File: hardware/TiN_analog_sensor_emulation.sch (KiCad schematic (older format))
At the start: 0 parts

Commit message: przeniosiono do folderu hardware
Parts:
- added H? (x4): MountingHole, symbol Mechanical:MountingHole
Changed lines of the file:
@@
 F11 "ADC7" O L 4300 4250 50
 F12 "ADC6" O L 4300 4150 50
+F13 "POTRST" O L 4300 3300 50
+F14 "POTSHDN" O L 4300 3400 50
 $EndSheet
 $Sheet
@@
 Wire Wire Line
 	3950 3150 4300 3150
+Wire Wire Line
+	3950 3300 4300 3300
+Wire Wire Line
+	4300 3400 3950 3400
+$Comp
+L Mechanical:MountingHole H?
+U 1 1 5D813031
+P 5550 1350
+F 0 "H?" H 5650 1396 50  0000 L CNN
+F 1 "MountingHole" H 5650 1305 50  0000 L CNN
+F 2 "" H 5550 1350 50  0001 C CNN
+F 3 "~" H 5550 1350 50  0001 C CNN
+	1    5550 1350
+	1    0    0    -1
+$EndComp
+$Comp
+L Mechanical:MountingHole H?
+U 1 1 5D8131EE
+P 5550 1150
+F 0 "H?" H 5650 1196 50  0000 L CNN
+F 1 "MountingHole" H 5650 1105 50  0000 L CNN
+F 2 "" H 5550 1150 50  0001 C CNN
+F 3 "~" H 5550 1150 50  0001 C CNN
+	1    5550 1150
+	1    0    0    -1
+$EndComp
+$Comp
+L Mechanical:MountingHole H?
+U 1 1 5D8138A8
+P 5550 950
+F 0 "H?" H 5650 996 50  0000 L CNN
+F 1 "MountingHole" H 5650 905 50  0000 L CNN
+F 2 "" H 5550 950 50  0001 C CNN
+F 3 "~" H 5550 950 50  0001 C CNN
+	1    5550 950
+	1    0    0    -1
+$EndComp
+$Comp
+L Mechanical:MountingHole H?
+U 1 1 5D8139A7
+P 5550 750
+F 0 "H?" H 5650 796 50  0000 L CNN
+F 1 "MountingHole" H 5650 705 50  0000 L CNN
+F 2 "" H 5550 750 50  0001 C CNN
+F 3 "~" H 5550 750 50  0001 C CNN
+	1    5550 750
+	1    0    0    -1
+$EndComp
 $EndSCHEMATC

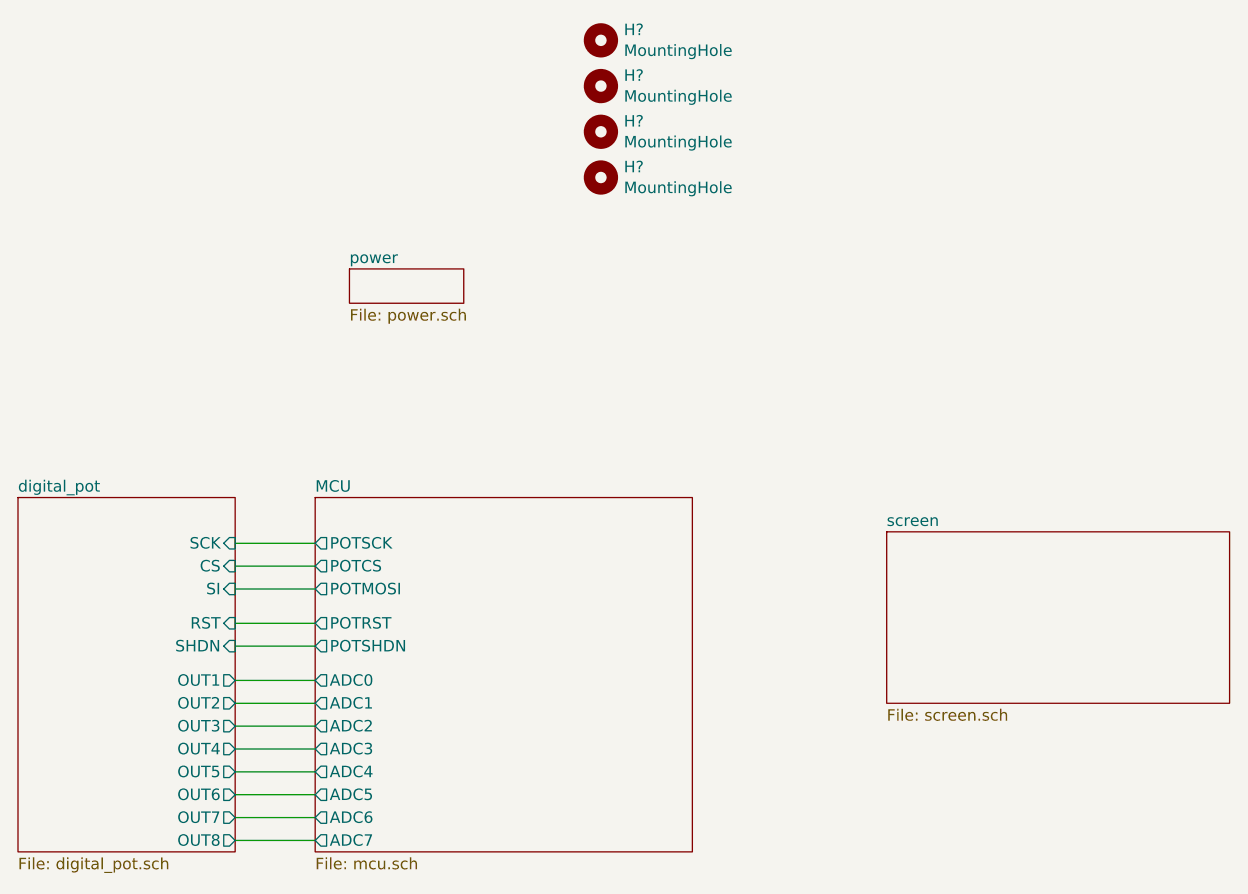
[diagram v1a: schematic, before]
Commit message: dodano wyjscie programatora, przyciski ustalono wysjcie i2c, dodany plik CubeMX z pinouterm
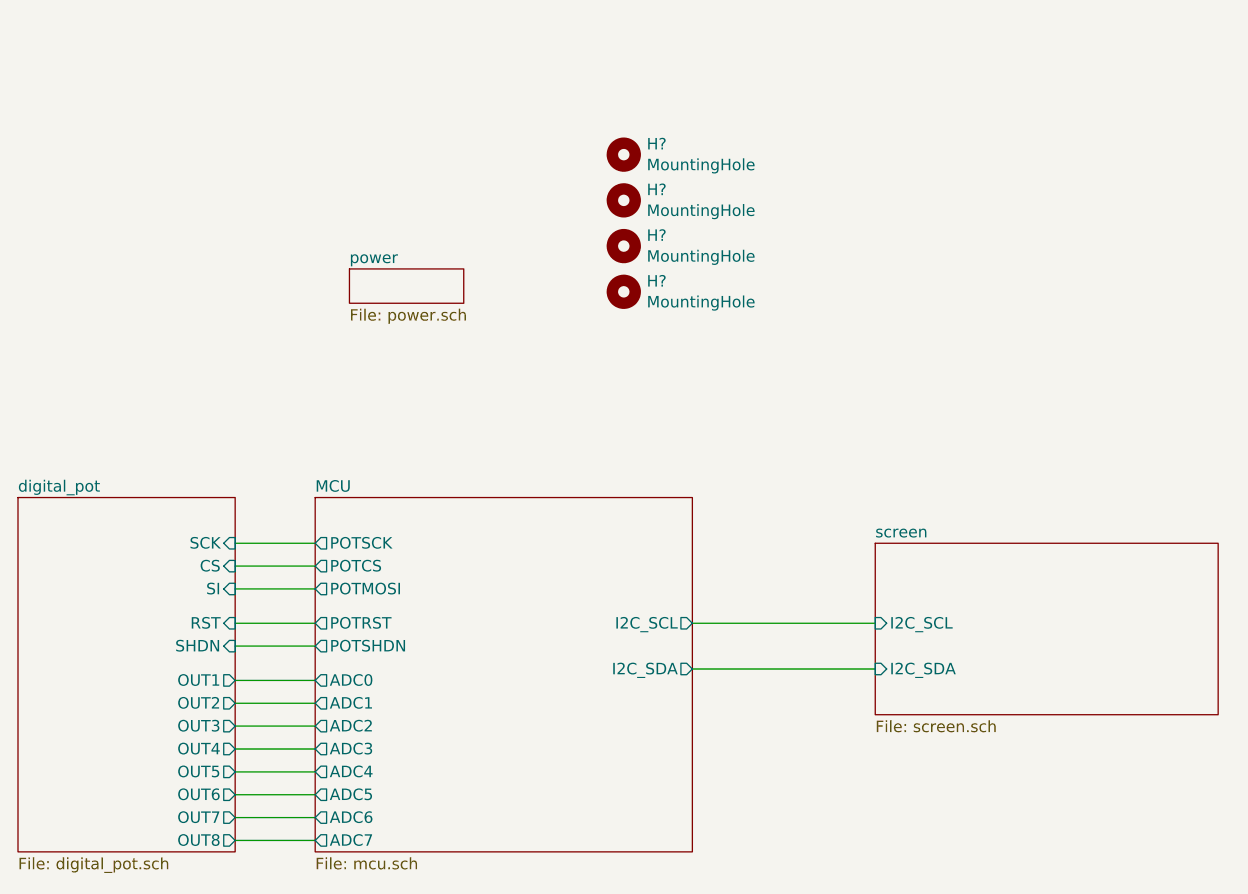
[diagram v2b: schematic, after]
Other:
- moved on the sheet: H?
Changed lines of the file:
@@
 F13 "POTRST" O L 4300 3300 50
 F14 "POTSHDN" O L 4300 3400 50
+F15 "I2C_SCL" O R 5950 3300 50
+F16 "I2C_SDA" O R 5950 3500 50
 $EndSheet
 $Sheet
@@
 $EndSheet
 $Sheet
-S 6800 2900 1500 750
+S 6750 2950 1500 750
 U 5CDEAC68
 F0 "screen" 50
 F1 "screen.sch" 50
+F2 "I2C_SCL" I L 6750 3300 50
+F3 "I2C_SDA" I L 6750 3500 50
 $EndSheet
 $Sheet
@@
 L Mechanical:MountingHole H?
 U 1 1 5D813031
-P 5550 1350
-F 0 "H?" H 5650 1396 50  0000 L CNN
-F 1 "MountingHole" H 5650 1305 50  0000 L CNN
-F 2 "" H 5550 1350 50  0001 C CNN
-F 3 "~" H 5550 1350 50  0001 C CNN
-	1    5550 1350
+P 5650 1850
+F 0 "H?" H 5750 1896 50  0000 L CNN
+F 1 "MountingHole" H 5750 1805 50  0000 L CNN
+F 2 "" H 5650 1850 50  0001 C CNN
+F 3 "~" H 5650 1850 50  0001 C CNN
+	1    5650 1850
 	1    0    0    -1
 $EndComp
@@
 L Mechanical:MountingHole H?
 U 1 1 5D8131EE
-P 5550 1150
-F 0 "H?" H 5650 1196 50  0000 L CNN
-F 1 "MountingHole" H 5650 1105 50  0000 L CNN
-F 2 "" H 5550 1150 50  0001 C CNN
-F 3 "~" H 5550 1150 50  0001 C CNN
-	1    5550 1150
+P 5650 1650
+F 0 "H?" H 5750 1696 50  0000 L CNN
+F 1 "MountingHole" H 5750 1605 50  0000 L CNN
+F 2 "" H 5650 1650 50  0001 C CNN
+F 3 "~" H 5650 1650 50  0001 C CNN
+	1    5650 1650
 	1    0    0    -1
 $EndComp
@@
 L Mechanical:MountingHole H?
 U 1 1 5D8138A8
-P 5550 950
-F 0 "H?" H 5650 996 50  0000 L CNN
-F 1 "MountingHole" H 5650 905 50  0000 L CNN
-F 2 "" H 5550 950 50  0001 C CNN
-F 3 "~" H 5550 950 50  0001 C CNN
-	1    5550 950
+P 5650 1450
+F 0 "H?" H 5750 1496 50  0000 L CNN
+F 1 "MountingHole" H 5750 1405 50  0000 L CNN
+F 2 "" H 5650 1450 50  0001 C CNN
+F 3 "~" H 5650 1450 50  0001 C CNN
+	1    5650 1450
 	1    0    0    -1
 $EndComp
@@
 L Mechanical:MountingHole H?
 U 1 1 5D8139A7
-P 5550 750
-F 0 "H?" H 5650 796 50  0000 L CNN
-F 1 "MountingHole" H 5650 705 50  0000 L CNN
-F 2 "" H 5550 750 50  0001 C CNN
-F 3 "~" H 5550 750 50  0001 C CNN
-	1    5550 750
+P 5650 1250
+F 0 "H?" H 5750 1296 50  0000 L CNN
+F 1 "MountingHole" H 5750 1205 50  0000 L CNN
+F 2 "" H 5650 1250 50  0001 C CNN
+F 3 "~" H 5650 1250 50  0001 C CNN
+	1    5650 1250
 	1    0    0    -1
 $EndComp
+Wire Wire Line
+	5950 3300 6750 3300
+Wire Wire Line
+	5950 3500 6750 3500
 $EndSCHEMATC

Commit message: DRC przechodzi dorzucone złącze do wyświetlacza na i2c oraz jeden push button
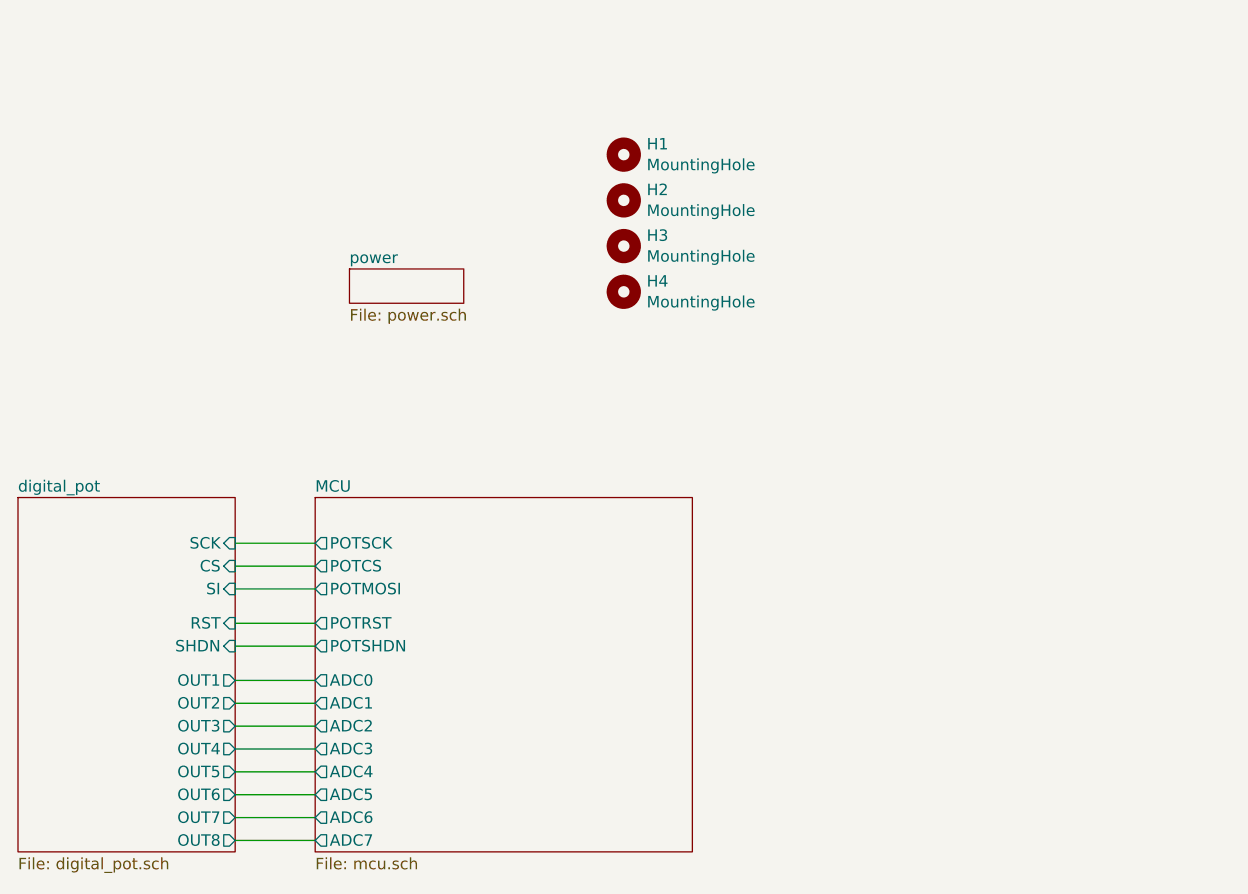
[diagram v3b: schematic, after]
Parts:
- gave numbers to parts that had none: 4
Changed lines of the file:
@@
 $Descr A4 11693 8268
 encoding utf-8
-Sheet 1 5
+Sheet 1 4
 Title ""
 Date ""
@@
 F13 "POTRST" O L 4300 3300 50
 F14 "POTSHDN" O L 4300 3400 50
-F15 "I2C_SCL" O R 5950 3300 50
-F16 "I2C_SDA" O R 5950 3500 50
 $EndSheet
 $Sheet
@@
 F13 "OUT7" O R 3950 4150 50
 F14 "OUT8" O R 3950 4250 50
-$EndSheet
-$Sheet
-S 6750 2950 1500 750
-U 5CDEAC68
-F0 "screen" 50
-F1 "screen.sch" 50
-F2 "I2C_SCL" I L 6750 3300 50
-F3 "I2C_SDA" I L 6750 3500 50
 $EndSheet
 $Sheet
@@
 	4300 3400 3950 3400
 $Comp
-L Mechanical:MountingHole H?
+L Mechanical:MountingHole H4
 U 1 1 5D813031
 P 5650 1850
-F 0 "H?" H 5750 1896 50  0000 L CNN
+F 0 "H4" H 5750 1896 50  0000 L CNN
 F 1 "MountingHole" H 5750 1805 50  0000 L CNN
 F 2 "" H 5650 1850 50  0001 C CNN
@@
 $EndComp
 $Comp
-L Mechanical:MountingHole H?
+L Mechanical:MountingHole H3
 U 1 1 5D8131EE
 P 5650 1650
-F 0 "H?" H 5750 1696 50  0000 L CNN
+F 0 "H3" H 5750 1696 50  0000 L CNN
 F 1 "MountingHole" H 5750 1605 50  0000 L CNN
 F 2 "" H 5650 1650 50  0001 C CNN
@@
 $EndComp
 $Comp
-L Mechanical:MountingHole H?
+L Mechanical:MountingHole H2
 U 1 1 5D8138A8
 P 5650 1450
-F 0 "H?" H 5750 1496 50  0000 L CNN
+F 0 "H2" H 5750 1496 50  0000 L CNN
 F 1 "MountingHole" H 5750 1405 50  0000 L CNN
 F 2 "" H 5650 1450 50  0001 C CNN
@@
 $EndComp
 $Comp
-L Mechanical:MountingHole H?
+L Mechanical:MountingHole H1
 U 1 1 5D8139A7
 P 5650 1250
-F 0 "H?" H 5750 1296 50  0000 L CNN
+F 0 "H1" H 5750 1296 50  0000 L CNN
 F 1 "MountingHole" H 5750 1205 50  0000 L CNN
 F 2 "" H 5650 1250 50  0001 C CNN
@@
 	1    0    0    -1
 $EndComp
-Wire Wire Line
-	5950 3300 6750 3300
-Wire Wire Line
-	5950 3500 6750 3500
 $EndSCHEMATC

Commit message: przypisano footprinty
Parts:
- H1, H2, H3, H4: footprint (none) -> MountingHole:MountingHole_3.2mm_M3
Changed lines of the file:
@@
 F 0 "H4" H 5750 1896 50  0000 L CNN
 F 1 "MountingHole" H 5750 1805 50  0000 L CNN
-F 2 "" H 5650 1850 50  0001 C CNN
+F 2 "MountingHole:MountingHole_3.2mm_M3" H 5650 1850 50  0001 C CNN
 F 3 "~" H 5650 1850 50  0001 C CNN
 	1    5650 1850
@@
 F 0 "H3" H 5750 1696 50  0000 L CNN
 F 1 "MountingHole" H 5750 1605 50  0000 L CNN
-F 2 "" H 5650 1650 50  0001 C CNN
+F 2 "MountingHole:MountingHole_3.2mm_M3" H 5650 1650 50  0001 C CNN
 F 3 "~" H 5650 1650 50  0001 C CNN
 	1    5650 1650
@@
 F 0 "H2" H 5750 1496 50  0000 L CNN
 F 1 "MountingHole" H 5750 1405 50  0000 L CNN
-F 2 "" H 5650 1450 50  0001 C CNN
+F 2 "MountingHole:MountingHole_3.2mm_M3" H 5650 1450 50  0001 C CNN
 F 3 "~" H 5650 1450 50  0001 C CNN
 	1    5650 1450
@@
 F 0 "H1" H 5750 1296 50  0000 L CNN
 F 1 "MountingHole" H 5750 1205 50  0000 L CNN
-F 2 "" H 5650 1250 50  0001 C CNN
+F 2 "MountingHole:MountingHole_3.2mm_M3" H 5650 1250 50  0001 C CNN
 F 3 "~" H 5650 1250 50  0001 C CNN
 	1    5650 1250

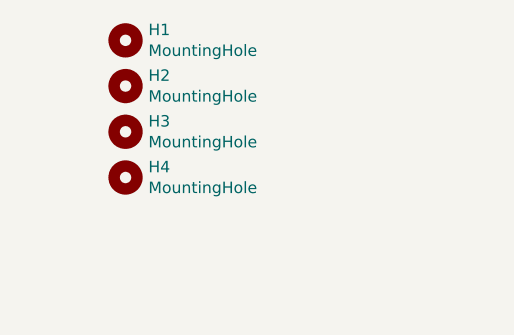
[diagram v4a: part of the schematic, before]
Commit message: dodany otwór do montażu wyświetlacza
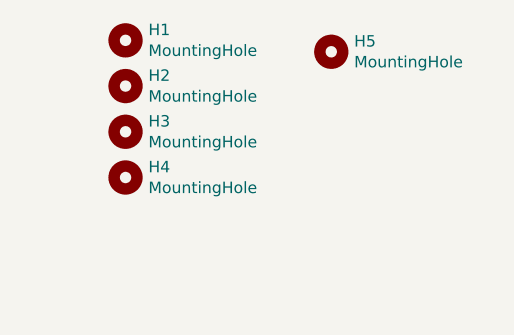
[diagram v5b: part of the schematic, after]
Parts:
- added H5: MountingHole, MountingHole:MountingHole_3.2mm_M3, symbol Mechanical:MountingHole
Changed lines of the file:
@@
+	1    0    0    -1
+$EndComp
+$Comp
+L Mechanical:MountingHole H5
+U 1 1 5D17B435
+P 6550 1300
+F 0 "H5" H 6650 1346 50  0000 L CNN
+F 1 "MountingHole" H 6650 1255 50  0000 L CNN
+F 2 "MountingHole:MountingHole_3.2mm_M3" H 6550 1300 50  0001 C CNN
+F 3 "~" H 6550 1300 50  0001 C CNN
+	1    6550 1300
 	1    0    0    -1
 $EndComp
